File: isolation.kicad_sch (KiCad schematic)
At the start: 38 parts, among them U1 UCC27517, U12 UCC24612, U3 ISO7710, U5 DPC817, U7 AMC0311R, U8 AMC0311R, U9 AMC0302R

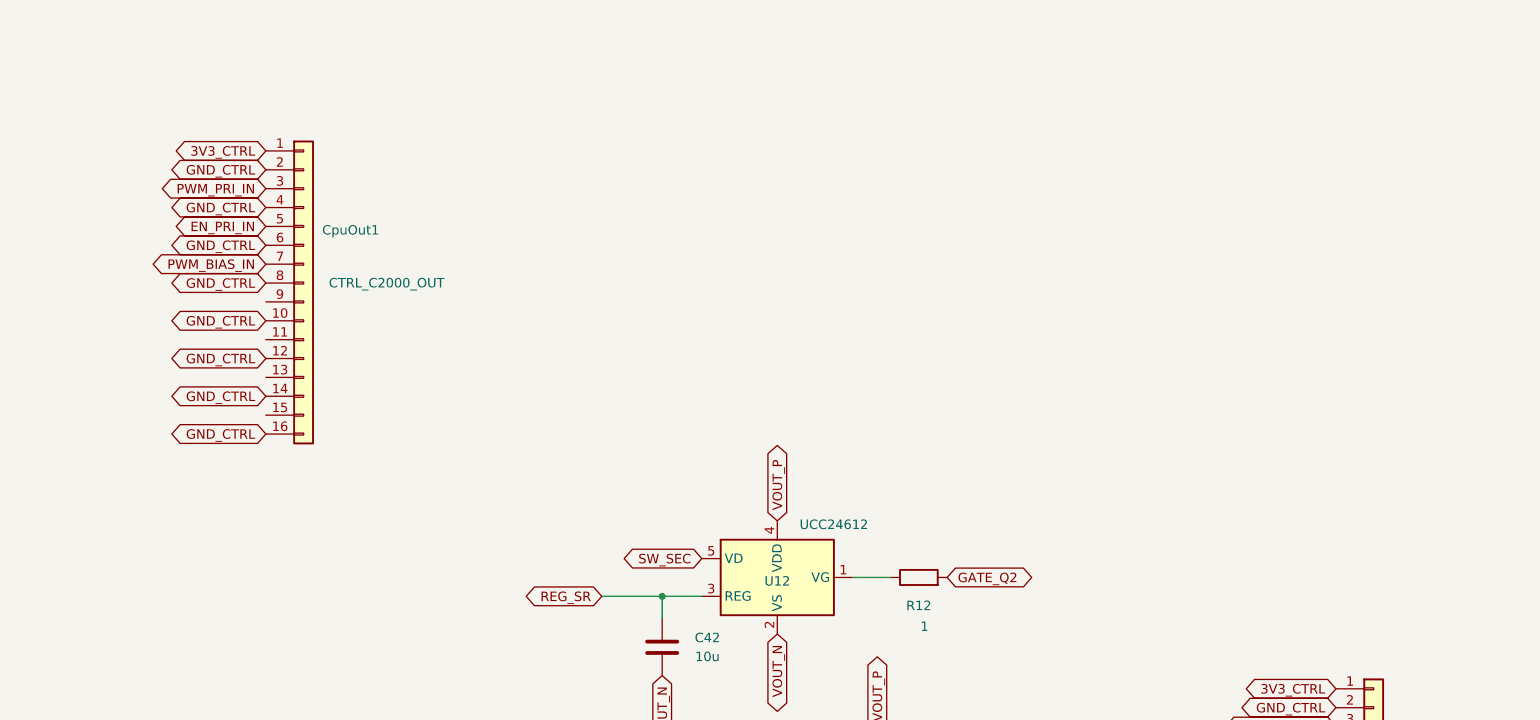
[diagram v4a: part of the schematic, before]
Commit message: Finalise le renommage alim-flyback-filament -> KICAD-HT et partage TO252
- Renommage du depot (fichiers deja renommes localement, jamais commite) :
  KICAD-HT.kicad_pcb/.kicad_pro/.kicad_sch, doc/KICAD-HT.png, references
  mises a jour (README.md, gen_composants.py PROJECT=, 00-intention-
  conception.md, doc/sim-vs-mesure.md, simulation/gen_asc.py).
  alim/isolation/polarisation.kicad_sch : resauvegarde native KiCad
  (reformatage), pas de changement electrique.
- bom_family_report.py : plus de chemin KiCad code en dur, detection
  dynamique du titre de projet (deja fait en session precedente, jamais
  commite).
- TO252 bascule vers la bibliotheque partagee lib_fp_commun/ (voir
  KICAD.md) : fp-lib-table pointe maintenant vers
  ${KIPRJMOD}/../lib_fp_commun/TO252.pretty au lieu de la copie locale,
  copie locale supprimee. Autres empreintes custom (A786, MSD1514,
  SOIC_DWV) : chemin de modele 3D repointe vers lib_fp_commun/ (les
  fichiers sources ont ete deplaces hors de composants-datasheets/datasheets/,
  qui ne garde plus que des PDF).

Co-Authored-By: Claude Sonnet 5 <noreply@anthropic.com>
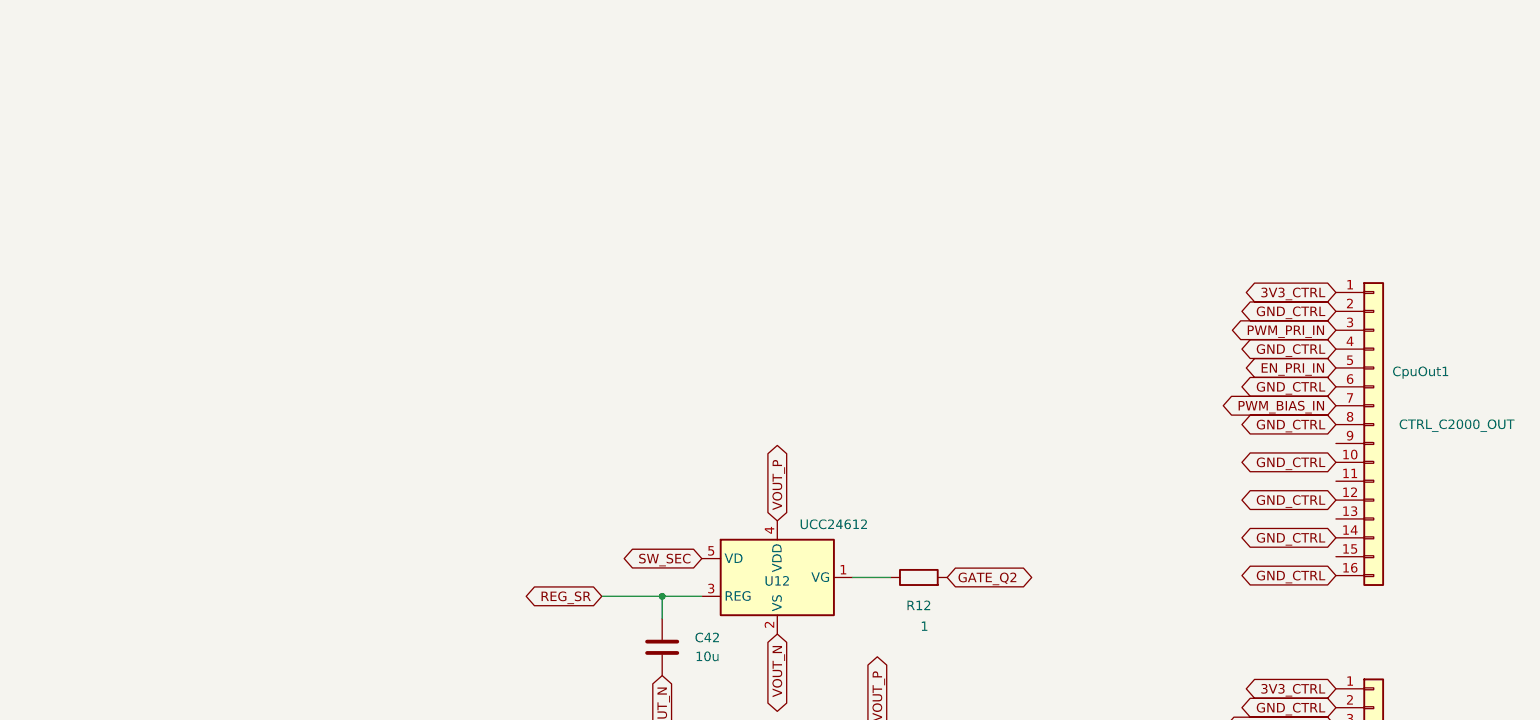
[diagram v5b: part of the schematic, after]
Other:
- moved on the sheet: CpuOut1

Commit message: Remplace CpuOut1/CpuIn1 par un connecteur J2 unique, aligné pin-a-pin sur J21 du shield
KICAD-C2000-powershield a desormais un connecteur IDC 2x10 dedie
(J21/NAPPE_FILAMENT_HT, decision #26) a la place du partage de nappes
generiques. J2 reprend exactement ce brochage ; 7 nets renommes pour
matcher le vocabulaire du shield (PWM_ht, PWM_EN, PWM_bias, Vht,
Temp_ht, I_Shunt_ht, V_bias, 3V3_ISO). GND_CTRL volontairement non
renomme en GND : KICAD-HT a deja un net GND distinct (masse primaire
non isolee), renommer aurait fusionne les deux domaines par coincidence
de nom. Vht_EN et I_Shunt_ht_comp poses mais non cables en interne
(reserve / futur trip rapide), par decision explicite.

ERC hierarchie complete : 0 erreur, 219 avertissements de la meme
famille qu'avant ce changement.

Co-Authored-By: Claude Sonnet 5 <noreply@anthropic.com>
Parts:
- removed CpuIn1: CTRL_C2000_IN, Connector_PinHeader_2.54mm:PinHeader_2x08_P2.54mm_Vertical, symbol Connector_Generic:Conn_01x16
- removed CpuOut1: CTRL_C2000_OUT, Connector_PinHeader_2.54mm:PinHeader_2x08_P2.54mm_Vertical, symbol Connector_Generic:Conn_01x16
- added J2: NAPPE_FILAMENT_HT, Connector_IDC:IDC-Header_2x10_P2.54mm_Vertical, symbol Connector_Generic:Conn_01x20
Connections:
- net GND_CTRL: now also J2.10 (Pin_10), J2.12 (Pin_12), J2.14 (Pin_14), J2.16 (Pin_16), J2.18 (Pin_18), J2.2 (Pin_2), J2.20 (Pin_20), J2.4 (Pin_4), J2.6 (Pin_6), J2.8 (Pin_8)
- net 3V3_CTRL renamed 3V3_ISO
- net 3V3_ISO: now also J2.1 (Pin_1)
- net EN_PRI_IN renamed PWM_EN
- net PWM_EN: now also J2.5 (Pin_5)
- net ISENSE_PRI_FBACK renamed I_Shunt_ht
- net I_Shunt_ht: now also J2.15 (Pin_15)
- net PWM_PRI_IN renamed PWM_ht
- net PWM_ht: now also J2.3 (Pin_3)
- net TEMP_PRI_FBACK renamed Temp_ht
- net Temp_ht: now also J2.13 (Pin_13)
- net VOUT_FBACK renamed Vht
- net Vht: now also J2.11 (Pin_11)
- new net I_Shunt_ht_comp: J2.17 (Pin_17)
- new net PWM_bias: J2.7 (Pin_7)
- new net V_bias: J2.19 (Pin_19)
- new net Vht_EN: J2.9 (Pin_9)

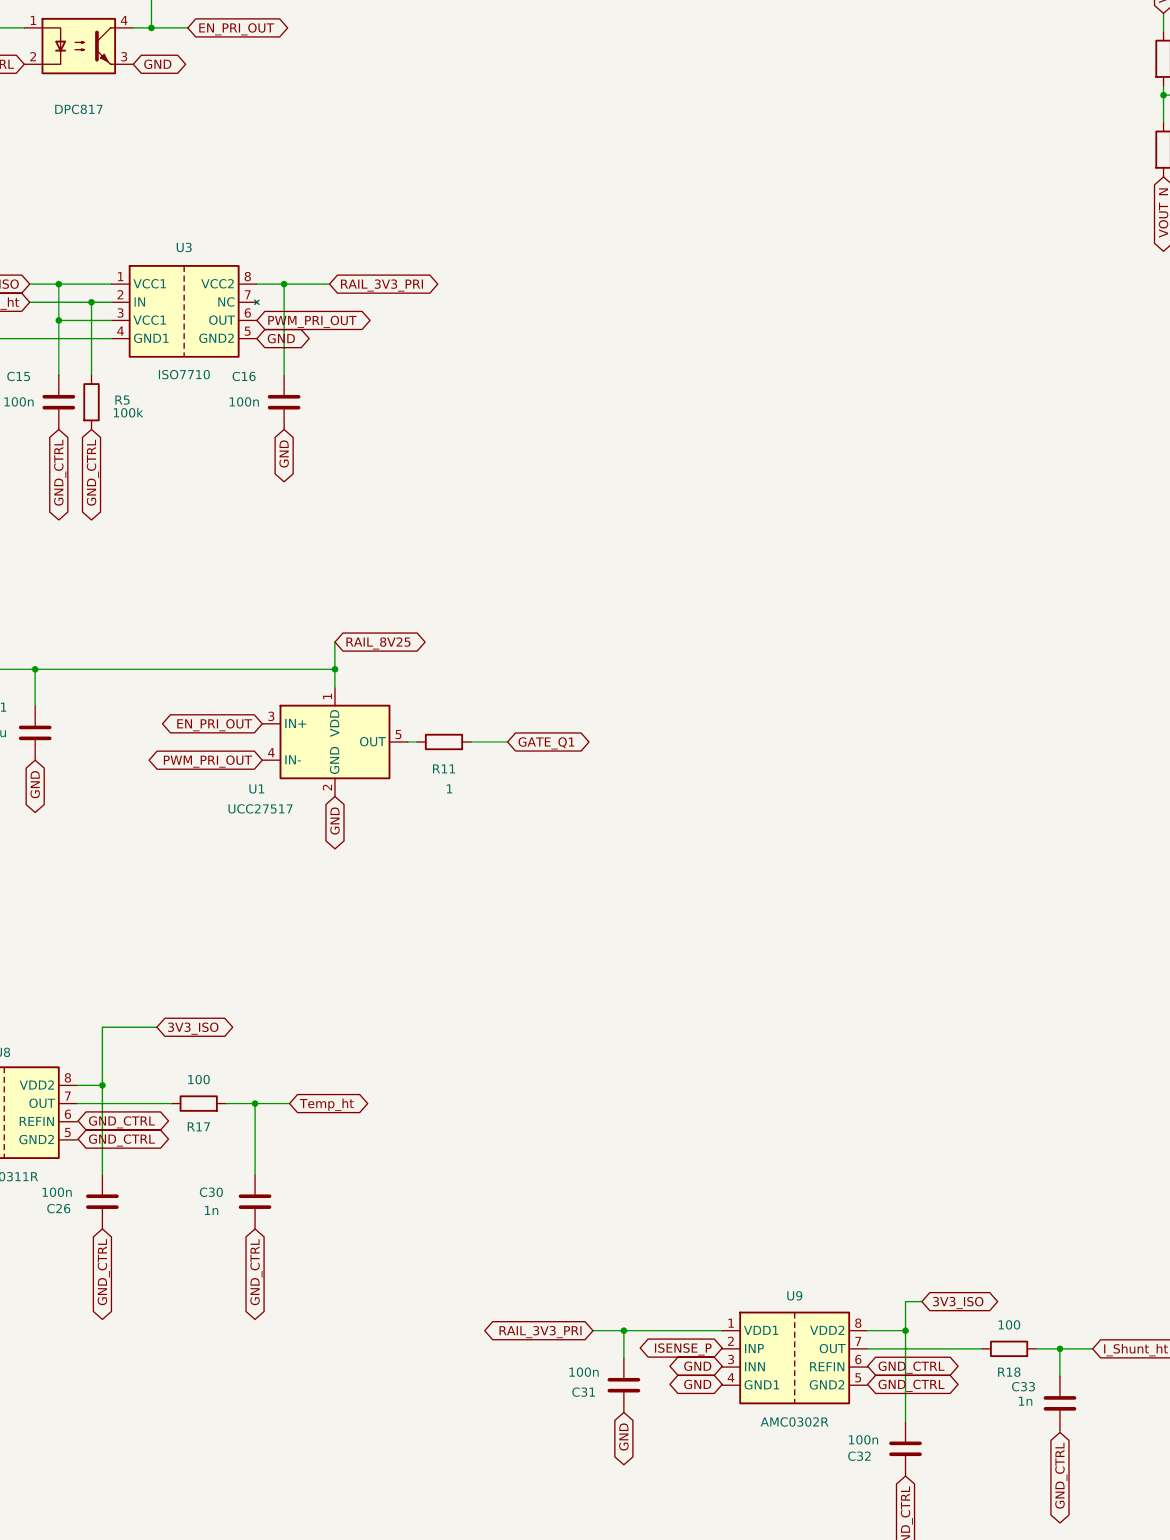
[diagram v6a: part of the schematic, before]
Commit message: Gate IN+ de U1 via un AND (SN74LVC1G08), U9 déplacé sur le Kelvin de R19
IN- de U1 est déjà occupé par PWM_PRI_OUT (pas disponible pour le
verrou comme le supposait le prompt de départ) : ajoute U13
(SN74LVC1G08), EN_PRI_GATED = EN_PRI_OUT AND nQ_TRIP, branché sur IN+ à
la place de EN_PRI_OUT direct. U3 non touché (ISO7710 reste ISO7710F
casserait le défaut-sûr actuel, voir 00-intention-conception.md §19).

U9 (AMC0302R) lit maintenant ISNS_KP/ISNS_KN (pastilles Kelvin de R19)
au lieu du chemin de puissance ISENSE_P/GND -- plus précis, gratuit une
fois le Kelvin disponible. Filtre de sortie R18/C33 retaillé
100R/1nF -> 1k/47nF pour réellement moyenner sur 200kHz (l'ancien
dimensionnement ne moyennait que du bruit HF, fc≈1,6MHz).

Co-Authored-By: Claude Sonnet 5 <noreply@anthropic.com>
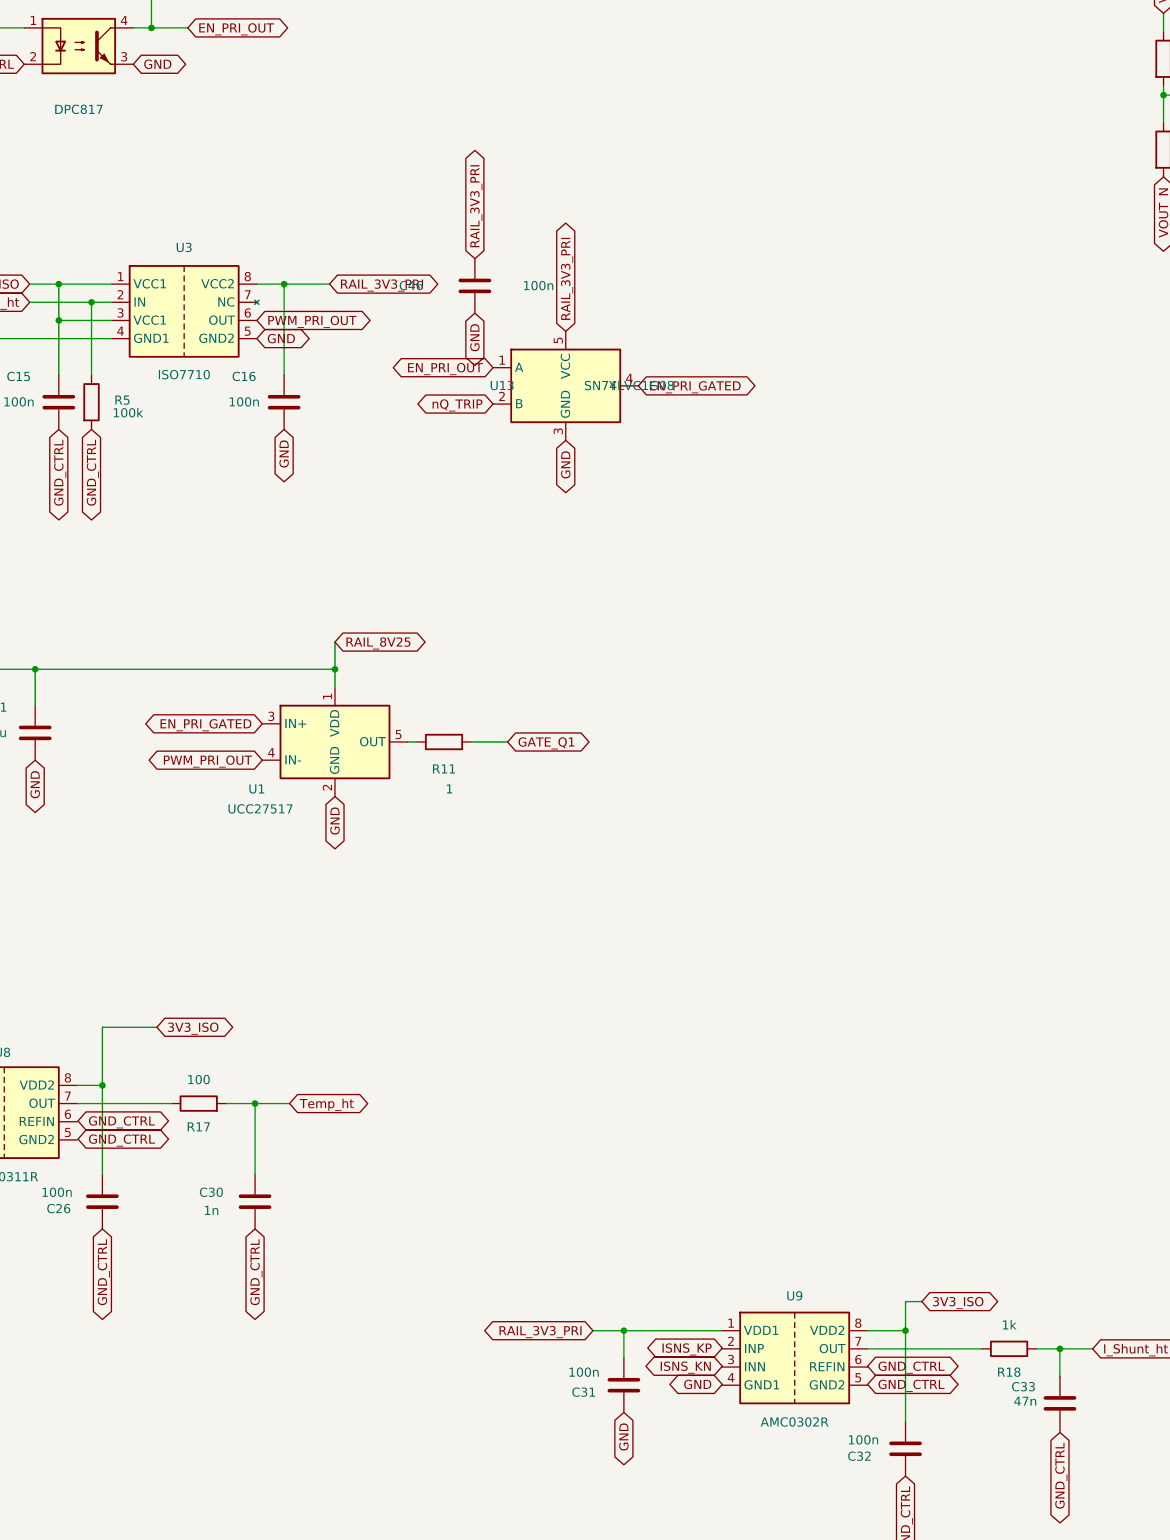
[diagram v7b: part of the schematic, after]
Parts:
- added C46: 100n, Capacitor_SMD:C_0805_2012Metric, symbol Device:C
- added U13: SN74LVC1G08, Package_TO_SOT_SMD:SOT-23-5, symbol custom_parts:SN74LVC1G08
- C33: value 1n -> 47n
- R18: value 100 -> 1k
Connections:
- net EN_PRI_OUT: now also U13.1 (A); no longer U1.3 (IN+)
- net GND: now also C46.2, U13.3 (GND); no longer U9.3 (INN)
- net RAIL_3V3_PRI: now also C46.1, U13.5 (VCC)
- net ISENSE_P renamed ISNS_KP
- new net EN_PRI_GATED: U1.3 (IN+), U13.4 (Y)
- new net ISNS_KN: U9.3 (INN)
- new net nQ_TRIP: U13.2 (B)
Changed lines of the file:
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@@
 		)
 	)
-	(global_label "GND"
+	(global_label "ISNS_KN"
 		(shape bidirectional)
 		(at 209.84 246.27 180)
@@
 		)
 	)
-	(global_label "ISENSE_P"
+	(global_label "ISNS_KP"
 		(shape bidirectional)
 		(at 209.84 243.73 180)
@@
 		)
 	)
-	(global_label "EN_PRI_OUT"
+	(global_label "EN_PRI_GATED"
 		(shape bidirectional)
 		(at 145.542 156.464 180)
@@
 			)
 		)
-		(property "Value" "100"
+		(property "Value" "1k"
 			(at 249.936 240.538 90)
 			(show_name no)
@@
 			)
 		)
-		(property "Value" "1n"
+		(property "Value" "47n"
 			(at 252.222 251.206 0)
 			(show_name no)
@@
 		)
 	)
+	(symbol
+		(lib_id "custom_parts:SN74LVC1G08")
+		(at 187.96 109.22 0)
+		(unit 1)
+		(exclude_from_sim no) (in_bom yes) (on_board yes) (dnp no)
+		(property "Reference" "U13" (at 179.07 109.22 0) (effects (font (size 1.27 1.27))))
+		(property "Value" "SN74LVC1G08" (at 196.85 109.22 0) (effects (font (size 1.27 1.27))))
+		(property "Footprint" "Package_TO_SOT_SMD:SOT-23-5" (at 187.96 109.22 0) (hide yes) (effects (font (size 1.27 1.27))))
+		(pin "5")
+		(pin "3")
+		(pin "1")
+		(pin "2")
+		(pin "4")
+		(instances
+			(project "KICAD-HT"
+				(path "/c8449ac7-87b3-4a93-889f-06dd686c5aff/2c364a36-1706-47ba-a3af-9fe08e477799" (reference "U13") (unit 1))
+			)
+		)
+	)
+	(symbol
+		(lib_id "Device:C")
+		(at 175.26 95.25 0)
+		(unit 1)
+		(exclude_from_sim no) (in_bom yes) (on_board yes) (dnp no)
+		(property "Reference" "C46" (at 166.37 95.25 0) (effects (font (size 1.27 1.27))))
+		(property "Value" "100n" (at 184.15 95.25 0) (effects (font (size 1.27 1.27))))
+		(property "Footprint" "Capacitor_SMD:C_0805_2012Metric" (at 175.26 95.25 0) (hide yes) (effects (font (size 1.27 1.27))))
+		(pin "1")
+		(pin "2")
+		(instances
+			(project "KICAD-HT"
+				(path "/c8449ac7-87b3-4a93-889f-06dd686c5aff/2c364a36-1706-47ba-a3af-9fe08e477799" (reference "C46") (unit 1))
+			)
+		)
+	)
+	(global_label "EN_PRI_OUT" (shape bidirectional) (at 177.80 106.68 180)
+		(fields_autoplaced yes)
+		(effects (font (size 1.27 1.27)) (justify right))
+	)
+	(global_label "nQ_TRIP" (shape bidirectional) (at 177.80 111.76 180)
+		(fields_autoplaced yes)
+		(effects (font (size 1.27 1.27)) (justify right))
+	)
+	(global_label "GND" (shape bidirectional) (at 187.96 116.84 270)
+		(fields_autoplaced yes)
+		(effects (font (size 1.27 1.27)) (justify right))
+	)
+	(global_label "EN_PRI_GATED" (shape bidirectional) (at 198.12 109.22 0)
+		(fields_autoplaced yes)
+		(effects (font (size 1.27 1.27)) (justify left))
+	)
+	(global_label "RAIL_3V3_PRI" (shape bidirectional) (at 187.96 101.60 90)
+		(fields_autoplaced yes)
+		(effects (font (size 1.27 1.27)) (justify left))
+	)
+	(global_label "RAIL_3V3_PRI" (shape bidirectional) (at 175.26 91.44 90)
+		(fields_autoplaced yes)
+		(effects (font (size 1.27 1.27)) (justify left))
+	)
+	(global_label "GND" (shape bidirectional) (at 175.26 99.06 270)
+		(fields_autoplaced yes)
+		(effects (font (size 1.27 1.27)) (justify right))
+	)
 )
